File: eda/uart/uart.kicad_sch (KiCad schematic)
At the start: 15 parts, among them J1 UART, U10 74HCT574, U15 74HCT00, U16 74HCT139, U18 74HCT32, U2 74HCT14, U6 74HCT08

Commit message: Branch of uart to v1
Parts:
- removed H1, H2: MountingHole, MountingHole:MountingHole_2.5mm, symbol Mechanical:MountingHole
- removed unit 6 of U2
- added H1, H2, H3, H4, H5, H6: MountingHole_Pad, MountingHole:MountingHole_2.5mm_Pad_Via, symbol Mechanical:MountingHole_Pad
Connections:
- net GND: now also H1.1, H2.1, H3.1, H4.1, H5.1, H6.1
- no-connect marks 8 -> 7

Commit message: Normalize cap size
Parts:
- C1, C15, C18, C19, C2, C21: footprint Capacitor_THT:C_Rect_L7.2mm_W3.5mm_P5.00mm_FKS2_FKP2_MKS2_MKP2 -> Capacitor_THT:C_Disc_D3.8mm_W2.6mm_P2.50mm
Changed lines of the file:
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@@
       (effects (font (size 1.27 1.27)) (justify left))
     )
-    (property "Footprint" "Capacitor_THT:C_Rect_L7.2mm_W3.5mm_P5.00mm_FKS2_FKP2_MKS2_MKP2" (at 149.5552 176.53 0)
+    (property "Footprint" "Capacitor_THT:C_Disc_D3.8mm_W2.6mm_P2.50mm" (at 149.5552 176.53 0)
       (effects (font (size 1.27 1.27)) hide)
     )
@@
       (effects (font (size 1.27 1.27)) (justify left))
     )
-    (property "Footprint" "Capacitor_THT:C_Rect_L7.2mm_W3.5mm_P5.00mm_FKS2_FKP2_MKS2_MKP2" (at 122.8852 176.53 0)
+    (property "Footprint" "Capacitor_THT:C_Disc_D3.8mm_W2.6mm_P2.50mm" (at 122.8852 176.53 0)
       (effects (font (size 1.27 1.27)) hide)
     )
@@
       (effects (font (size 1.27 1.27)) (justify left))
     )
-    (property "Footprint" "Capacitor_THT:C_Rect_L7.2mm_W3.5mm_P5.00mm_FKS2_FKP2_MKS2_MKP2" (at 18.7452 175.895 0)
+    (property "Footprint" "Capacitor_THT:C_Disc_D3.8mm_W2.6mm_P2.50mm" (at 18.7452 175.895 0)
       (effects (font (size 1.27 1.27)) hide)
     )
@@
       (effects (font (size 1.27 1.27)) (justify left))
     )
-    (property "Footprint" "Capacitor_THT:C_Rect_L7.2mm_W3.5mm_P5.00mm_FKS2_FKP2_MKS2_MKP2" (at 55.5752 175.895 0)
+    (property "Footprint" "Capacitor_THT:C_Disc_D3.8mm_W2.6mm_P2.50mm" (at 55.5752 175.895 0)
       (effects (font (size 1.27 1.27)) hide)
     )
@@
       (effects (font (size 1.27 1.27)) (justify left))
     )
-    (property "Footprint" "Capacitor_THT:C_Rect_L7.2mm_W3.5mm_P5.00mm_FKS2_FKP2_MKS2_MKP2" (at 93.0402 175.895 0)
+    (property "Footprint" "Capacitor_THT:C_Disc_D3.8mm_W2.6mm_P2.50mm" (at 93.0402 175.895 0)
       (effects (font (size 1.27 1.27)) hide)
     )
@@
       (effects (font (size 1.27 1.27)) (justify left))
     )
-    (property "Footprint" "Capacitor_THT:C_Rect_L7.2mm_W3.5mm_P5.00mm_FKS2_FKP2_MKS2_MKP2" (at 272.7452 53.34 0)
-      (effects (font (size 1.27 1.27)) hide)
-    )
+    (property "Footprint" "Capacitor_THT:C_Disc_D3.8mm_W2.6mm_P2.50mm" (at 272.7452 53.34 0)
+      (effects (font (size 1.27 1.27)) hide)
+    )

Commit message: Uart and loader work
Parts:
- renumbered U6 to U1, U16 to U7
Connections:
- net GND: now also U10.3 (D1), U10.4 (D2); no longer U10.8 (D6), U10.9 (D7)
- net recieve/DataAvailable: now also U10.9 (D7); no longer U10.4 (D2)
- net recieve/RecieveBufferFull: now also U10.2 (D0); no longer U10.3 (D1)
- net transmit/InputBufferFull: now also U10.8 (D6); no longer U10.2 (D0)

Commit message: Uart eda work
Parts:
- removed J1: UART, Connector_PinHeader_2.54mm:PinHeader_1x03_P2.54mm_Horizontal, symbol Connector:Conn_01x03_Pin
- added C22: 0.1uf, Capacitor_THT:C_Disc_D3.8mm_W2.6mm_P2.50mm, symbol Device:C
- added J1: RX/TX Con, Connector_PinHeader_2.54mm:PinHeader_1x04_P2.54mm_Horizontal, symbol Connector:Conn_01x04_Pin
- added JP9: IRQ Disconnect, Connector_PinHeader_2.54mm:PinHeader_1x02_P2.54mm_Vertical, symbol Jumper:Jumper_2_Bridged
- added U19: 74HCT74, Package_DIP:DIP-14_W7.62mm, symbol 74xx:74HC74
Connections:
- net Expansion header/~{IRQ}: now also JP9.1 (A)
- net GND: now also C22.2, J1.4 (Pin_4), U19.11 (C), U19.12 (D), U19.7 (GND); no longer U10.3 (D1), U15.4, U15.5
- net VCC: now also C22.1, U19.14 (VCC)
- net recieve/DataAvailable: now also U15.4
- net recieve/RX: now also J1.3 (Pin_3)
- net transmit/TX: now also J1.2 (Pin_2)
- net at U15.6: now also U19.10 (~{S})
- new net: U10.3 (D1), U19.9 (Q)
- new net: JP9.2 (B), U19.8 (~{Q})
- new net address_decode/IrqActive: U15.5
- new net address_decode/~{DeviceEnable}: U19.13 (~{R})
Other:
- sheet address_decode ports: added D0, IrqActive, ~{DeviceEnable}, ~{RST}; removed none
- moved on the sheet: C1, C18, C19, C21, U15B, U15E, U16C, U18C, U18D, U18E, U1E, U2C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

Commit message: UART routing pass 1
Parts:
- removed H1, H2: MountingHole_Pad, MountingHole:MountingHole_2.5mm_Pad_Via, symbol Mechanical:MountingHole_Pad
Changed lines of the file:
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@@
 	)
 	(junction
-		(at 146.05 60.96)
+		(at 148.59 30.48)
 		(diameter 0)
 		(color 0 0 0 0)
 	)
 	(junction
-		(at 255.27 118.11)
+		(at 146.05 60.96)
 		(diameter 0)
 		(color 0 0 0 0)
 	)
 	(junction
-		(at 39.878 101.346)
+		(at 255.27 118.11)
 		(diameter 0)
 		(color 0 0 0 0)
@@
 	)
 	(junction
-		(at 39.878 110.49)
+		(at 100.33 39.37)
 		(diameter 0)
 		(color 0 0 0 0)
 	)
 	(junction
-		(at 100.33 39.37)
+		(at 148.59 19.05)
 		(diameter 0)
 		(color 0 0 0 0)
@@
 	(wire
 		(pts
-			(xy 39.878 92.202) (xy 39.878 101.346)
-		)
-		(stroke
-			(width 0)
-			(type default)
-		)
-	)
-	(wire
-		(pts
 			(xy 102.87 156.21) (xy 102.87 157.48)
 		)
@@
 		)
 	)
+	(bus
+		(pts
+			(xy 148.59 30.48) (xy 148.59 57.15)
+		)
+		(stroke
+			(width 0)
+			(type default)
+		)
+	)
 	(wire
 		(pts
@@
 	(bus
 		(pts
-			(xy 95.25 19.05) (xy 262.89 19.05)
+			(xy 95.25 19.05) (xy 148.59 19.05)
 		)
 		(stroke
@@
 	(wire
 		(pts
-			(xy 39.878 101.346) (xy 39.878 110.49)
-		)
-		(stroke
-			(width 0)
-			(type default)
-		)
-	)
-	(wire
-		(pts
 			(xy 115.57 157.48) (xy 115.57 167.64)
 		)
@@
 	(wire
 		(pts
-			(xy 29.464 92.202) (xy 39.878 92.202)
-		)
-		(stroke
-			(width 0)
-			(type default)
-		)
-	)
-	(wire
-		(pts
 			(xy 39.878 119.888) (xy 39.878 129.286)
 		)
@@
 	(bus
 		(pts
-			(xy 148.59 19.05) (xy 148.59 57.15)
+			(xy 148.59 19.05) (xy 148.59 30.48)
 		)
 		(stroke
@@
 		)
 	)
-	(wire
+	(bus
 		(pts
-			(xy 29.464 101.346) (xy 39.878 101.346)
+			(xy 148.59 19.05) (xy 262.89 19.05)
 		)
 		(stroke
@@
 	)
 	(symbol
-		(lib_id "Mechanical:MountingHole_Pad")
-		(at 26.924 101.346 90)
-		(unit 1)
-		(exclude_from_sim no)
-		(in_bom yes)
-		(on_board yes)
-		(dnp no)
-		(fields_autoplaced yes)
-		(property "Reference" "H2"
-			(at 25.654 95.504 90)
-			(effects
-				(font
-					(size 1.27 1.27)
-				)
-			)
-		)
-		(property "Value" "MountingHole_Pad"
-			(at 25.654 98.044 90)
-			(effects
-				(font
-					(size 1.27 1.27)
-				)
-			)
-		)
-		(property "Footprint" "MountingHole:MountingHole_2.5mm_Pad_Via"
-			(at 26.924 101.346 0)
-			(effects
-				(font
-					(size 1.27 1.27)
-				)
-				(hide yes)
-			)
-		)
-		(property "Datasheet" "~"
-			(at 26.924 101.346 0)
-			(effects
-				(font
-					(size 1.27 1.27)
-				)
-				(hide yes)
-			)
-		)
-		(property "Description" ""
-			(at 26.924 101.346 0)
-			(effects
-				(font
-					(size 1.27 1.27)
-				)
-				(hide yes)
-			)
-		)
-		(pin "1"
-		)
-		(instances
-			(project "uart"
-				(path "/11545594-d6d6-4b37-a578-fa23933d5773"
-					(reference "H2")
-					(unit 1)
-				)
-			)
-		)
-	)
-	(symbol
 		(lib_id "power:GND")
 		(at 45.72 67.31 270)
@@
 					(unit 1)
 				)
-			)
-		)
-	)
-	(symbol
-		(lib_id "Mechanical:MountingHole_Pad")
-		(at 26.924 92.202 90)
-		(unit 1)
-		(exclude_from_sim no)
-		(in_bom yes)
-		(on_board yes)
-		(dnp no)
-		(fields_autoplaced yes)
-		(property "Reference" "H1"
-			(at 25.654 86.36 90)
-			(effects
-				(font
-					(size 1.27 1.27)
-				)
-			)
-		)
-		(property "Value" "MountingHole_Pad"
-			(at 25.654 88.9 90)
-			(effects
-				(font
-					(size 1.27 1.27)
-				)
-			)
-		)
-		(property "Footprint" "MountingHole:MountingHole_2.5mm_Pad_Via"
-			(at 26.924 92.202 0)
-			(effects
-				(font
-					(size 1.27 1.27)
-				)
-				(hide yes)
-			)
-		)
-		(property "Datasheet" "~"
-			(at 26.924 92.202 0)
-			(effects
-				(font
-					(size 1.27 1.27)
-				)
-				(hide yes)
-			)
-		)
-		(property "Description" ""
-			(at 26.924 92.202 0)
-			(effects
-				(font
-					(size 1.27 1.27)
-				)
-				(hide yes)
-			)
-		)
-		(pin "1"
-		)
-		(instances
-			(project "uart"
-				(path "/11545594-d6d6-4b37-a578-fa23933d5773"
-					(reference "H1")
-					(unit 1)
-				)

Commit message: Uart latch logic
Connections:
- net Expansion header/Clock: now also U7.14 (A0); no longer U10.11 (Cp)
- net GND: now also U7.15 (E); no longer U7.14 (A0)
- net VCC: no longer U7.15 (E)
- net at U7.11 (O1): now also U10.11 (Cp)
- no-connect marks 7 -> 6
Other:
- moved on the sheet: U7B
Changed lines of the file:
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@@
 	)
 	(junction
+		(at 224.79 99.06)
+		(diameter 0)
+		(color 0 0 0 0)
+	)
+	(junction
 		(at 148.59 30.48)
 		(diameter 0)
@@
 	)
 	(junction
-		(at 255.27 142.24)
-		(diameter 0)
-		(color 0 0 0 0)
-	)
-	(junction
 		(at 102.87 185.42)
 		(diameter 0)
@@
 	)
 	(junction
-		(at 255.27 139.7)
-		(diameter 0)
-		(color 0 0 0 0)
-	)
-	(junction
 		(at 223.52 48.26)
 		(diameter 0)
@@
 	)
 	(no_connect
-		(at 283.21 142.24)
+		(at 251.46 91.44)
 	)
 	(no_connect
@@
 	)
 	(no_connect
-		(at 283.21 144.78)
-	)
-	(no_connect
-		(at 283.21 147.32)
+		(at 251.46 96.52)
 	)
 	(no_connect
-		(at 283.21 139.7)
+		(at 251.46 99.06)
 	)
 	(no_connect
@@
 	(wire
 		(pts
+			(xy 233.68 82.55) (xy 255.27 82.55)
+		)
+		(stroke
+			(width 0)
+			(type default)
+		)
+	)
+	(wire
+		(pts
 			(xy 130.81 185.42) (xy 130.81 186.69)
 		)
@@
 	(wire
 		(pts
+			(xy 226.06 60.96) (xy 224.79 60.96)
+		)
+		(stroke
+			(width 0)
+			(type default)
+		)
+	)
+	(wire
+		(pts
 			(xy 77.47 62.23) (xy 80.01 62.23)
 		)
@@
 	(wire
 		(pts
+			(xy 224.79 99.06) (xy 226.06 99.06)
+		)
+		(stroke
+			(width 0)
+			(type default)
+		)
+	)
+	(wire
+		(pts
 			(xy 146.05 34.29) (xy 146.05 60.96)
 		)
@@
 	(wire
 		(pts
-			(xy 255.27 142.24) (xy 255.27 158.75)
+			(xy 255.27 130.81) (xy 255.27 158.75)
 		)
 		(stroke
@@
 	(wire
 		(pts
+			(xy 226.06 90.17) (xy 222.25 90.17)
+		)
+		(stroke
+			(width 0)
+			(type default)
+		)
+	)
+	(wire
+		(pts
+			(xy 222.25 90.17) (xy 222.25 93.98)
+		)
+		(stroke
+			(width 0)
+			(type default)
+		)
+	)
+	(wire
+		(pts
+			(xy 233.68 78.74) (xy 233.68 82.55)
+		)
+		(stroke
+			(width 0)
+			(type default)
+		)
+	)
+	(wire
+		(pts
+			(xy 224.79 99.06) (xy 224.79 104.14)
+		)
+		(stroke
+			(width 0)
+			(type default)
+		)
+	)
+	(wire
+		(pts
 			(xy 255.27 125.73) (xy 255.27 130.81)
 		)
@@
 	(wire
 		(pts
-			(xy 200.66 80.01) (xy 200.66 60.96)
+			(xy 224.79 91.44) (xy 224.79 99.06)
 		)
 		(stroke
@@
 	(wire
 		(pts
-			(xy 255.27 139.7) (xy 255.27 142.24)
-		)
-		(stroke
-			(width 0)
-			(type default)
-		)
-	)
-	(wire
-		(pts
 			(xy 80.01 62.23) (xy 81.28 62.23)
 		)
@@
 	(wire
 		(pts
-			(xy 200.66 60.96) (xy 226.06 60.96)
-		)
-		(stroke
-			(width 0)
-			(type default)
-		)
-	)
-	(wire
-		(pts
 			(xy 54.61 113.03) (xy 69.85 113.03)
 		)
@@
 	(wire
 		(pts
-			(xy 255.27 139.7) (xy 257.81 139.7)
-		)
-		(stroke
-			(width 0)
-			(type default)
-		)
-	)
-	(wire
-		(pts
 			(xy 102.87 157.48) (xy 102.87 158.75)
 		)
@@
 	(wire
 		(pts
-			(xy 255.27 130.81) (xy 255.27 139.7)
-		)
-		(stroke
-			(width 0)
-			(type default)
-		)
-	)
-	(wire
-		(pts
 			(xy 44.45 25.4) (xy 48.26 25.4)
 		)
@@
 	(wire
 		(pts
-			(xy 255.27 142.24) (xy 257.81 142.24)
+			(xy 255.27 82.55) (xy 255.27 93.98)
 		)
 		(stroke
@@
 	(wire
 		(pts
-			(xy 100.33 80.01) (xy 200.66 80.01)
+			(xy 100.33 80.01) (xy 226.06 80.01)
 		)
 		(stroke
@@
 	(wire
 		(pts
+			(xy 224.79 78.74) (xy 233.68 78.74)
+		)
+		(stroke
+			(width 0)
+			(type default)
+		)
+	)
+	(wire
+		(pts
 			(xy 238.76 73.66) (xy 238.76 72.39)
 		)
@@
 	(wire
 		(pts
+			(xy 251.46 93.98) (xy 255.27 93.98)
+		)
+		(stroke
+			(width 0)
+			(type default)
+		)
+	)
+	(wire
+		(pts
+			(xy 222.25 93.98) (xy 226.06 93.98)
+		)
+		(stroke
+			(width 0)
+			(type default)
+		)
+	)
+	(wire
+		(pts
 			(xy 156.21 182.88) (xy 156.21 185.42)
 		)
@@
 		)
 	)
+	(wire
+		(pts
+			(xy 226.06 91.44) (xy 224.79 91.44)
+		)
+		(stroke
+			(width 0)
+			(type default)
+		)
+	)
+	(wire
+		(pts
+			(xy 224.79 60.96) (xy 224.79 78.74)
+		)
+		(stroke
+			(width 0)
+			(type default)
+		)
+	)
 	(bus
 		(pts
@@
 		)
 	)
+	(wire
+		(pts
+			(xy 226.06 80.01) (xy 226.06 90.17)
+		)
+		(stroke
+			(width 0)
+			(type default)
+		)
+	)
 	(label "D5"
 		(at 251.46 50.8 0)
@@
 	(label "D0"
 		(at 100.33 26.67 0)
+		(fields_autoplaced yes)
 		(effects
 			(font
@@
 	)
 	(symbol
-		(lib_id "power:VCC")
-		(at 257.81 147.32 180)
-		(unit 1)
-		(exclude_from_sim no)
-		(in_bom yes)
-		(on_board yes)
-		(dnp no)
-		(fields_autoplaced yes)
-		(property "Reference" "#PWR053"
-			(at 257.81 143.51 0)
-			(effects
-				(font
-					(size 1.27 1.27)
-				)
-				(hide yes)
-			)
-		)
-		(property "Value" "VCC"
-			(at 257.81 152.4 0)
-			(effects
-				(font
-					(size 1.27 1.27)
-				)
-			)
-		)
-		(property "Footprint" ""
-			(at 257.81 147.32 0)
-			(effects
-				(font
-					(size 1.27 1.27)
-				)
-				(hide yes)
-			)
-		)
-		(property "Datasheet" ""
-			(at 257.81 147.32 0)
-			(effects
-				(font
-					(size 1.27 1.27)
-				)
-				(hide yes)
-			)
-		)
-		(property "Description" ""
-			(at 257.81 147.32 0)
-			(effects
-				(font
-					(size 1.27 1.27)
-				)
-				(hide yes)
-			)
-		)
-		(pin "1"
-		)
-		(instances
-			(project "uart"
-				(path "/11545594-d6d6-4b37-a578-fa23933d5773"
-					(reference "#PWR053")
-					(unit 1)
-				)
-			)
-		)
-	)
-	(symbol
 		(lib_id "power:GND")
 		(at 69.85 142.24 0)
@@
 	(symbol
 		(lib_id "74xx:74LS139")
-		(at 270.51 142.24 0)
+		(at 238.76 93.98 0)
 		(unit 2)
 		(exclude_from_sim no)
@@
 		(fields_autoplaced yes)
 		(property "Reference" "U7"
-			(at 270.51 133.35 0)
+			(at 238.76 85.09 0)
 			(effects
 				(font
@@
 		)
 		(property "Value" "74HCT139"
-			(at 270.51 135.89 0)
+			(at 238.76 87.63 0)
 			(effects
 				(font
@@
 		)
 		(property "Footprint" "Package_DIP:DIP-16_W7.62mm"
-			(at 270.51 142.24 0)
+			(at 238.76 93.98 0)
 			(effects
 				(font
@@
 		)
 		(property "Datasheet" "http://www.ti.com/lit/ds/symlink/sn74ls139a.pdf"
-			(at 270.51 142.24 0)
+			(at 238.76 93.98 0)
 			(effects
 				(font
@@
 		)
 		(property "Description" ""
-			(at 270.51 142.24 0)
+			(at 238.76 93.98 0)
 			(effects
 				(font
@@
 					(unit 1)
 				)
+			)
+		)
+	)
+	(symbol
+		(lib_id "power:GND")
+		(at 224.79 104.14 0)
+		(unit 1)
+		(exclude_from_sim no)
+		(in_bom yes)
+		(on_board yes)
+		(dnp no)
+		(fields_autoplaced yes)
+		(property "Reference" "#PWR053"
+			(at 224.79 110.49 0)
+			(effects
+				(font
+					(size 1.27 1.27)
+				)
+				(hide yes)
+			)
+		)
+		(property "Value" "GND"
+			(at 224.79 109.22 0)
+			(effects
+				(font
+					(size 1.27 1.27)
+				)
+			)
+		)
+		(property "Footprint" ""
+			(at 224.79 104.14 0)
+			(effects
+				(font
+					(size 1.27 1.27)
+				)
+				(hide yes)
+			)
+		)
+		(property "Datasheet" ""
+			(at 224.79 104.14 0)
+			(effects
+				(font
+					(size 1.27 1.27)
+				)
+				(hide yes)
+			)
+		)
+		(property "Description" ""
+			(at 224.79 104.14 0)
+			(effects
+				(font
+					(size 1.27 1.27)
+				)
+				(hide yes)
+			)
+		)
+		(pin "1"
+		)
+		(instances
+			(project "uart"
+				(path "/11545594-d6d6-4b37-a578-fa23933d5773"
+					(reference "#PWR053")
+					(unit 1)
+				)

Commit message: Touchups before ordering
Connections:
- net recieve/RX: now also J1.2 (Pin_2); no longer J1.3 (Pin_3)
- net transmit/TX: now also J1.3 (Pin_3); no longer J1.2 (Pin_2)

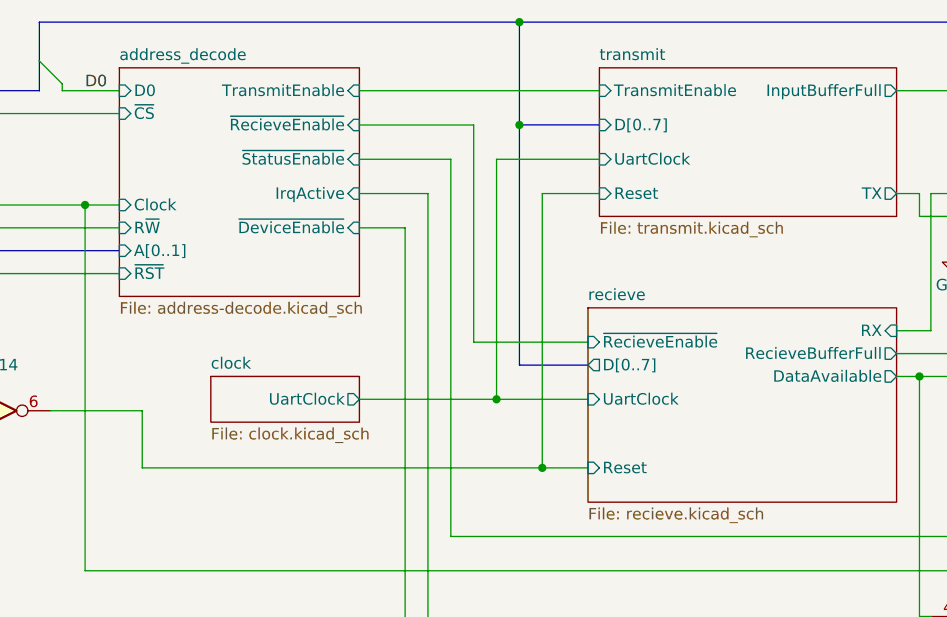
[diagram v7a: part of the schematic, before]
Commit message: Uart board to v1.1...make bodges permanent :(
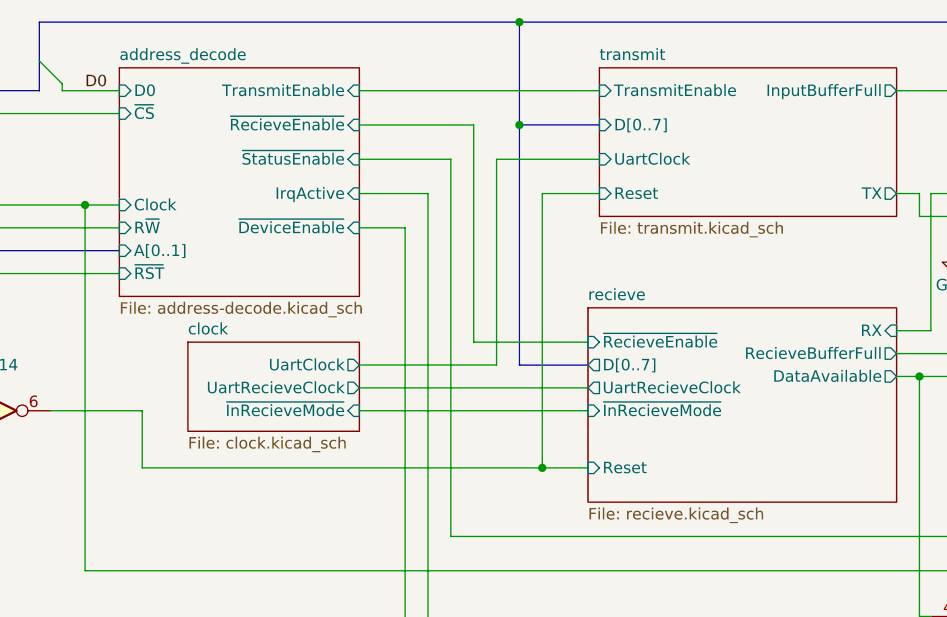
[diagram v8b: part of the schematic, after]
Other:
- sheet clock ports: added UartRecieveClock, ~{InRecieveMode}; removed none
- sheet recieve ports: added UartRecieveClock, ~{InRecieveMode}; removed UartClock
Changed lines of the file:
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@@
 	)
 	(junction
-		(at 146.05 60.96)
-		(diameter 0)
-		(color 0 0 0 0)
-	)
-	(junction
 		(at 255.27 118.11)
 		(diameter 0)
@@
 	(wire
 		(pts
-			(xy 146.05 60.96) (xy 156.21 60.96)
-		)
-		(stroke
-			(width 0)
-			(type default)
-		)
-	)
-	(wire
-		(pts
 			(xy 190.5 55.88) (xy 215.9 55.88)
 		)
@@
 	(wire
 		(pts
-			(xy 146.05 34.29) (xy 146.05 60.96)
+			(xy 146.05 34.29) (xy 146.05 57.15)
 		)
 		(stroke
@@
 	(wire
 		(pts
-			(xy 130.81 60.96) (xy 146.05 60.96)
+			(xy 130.81 57.15) (xy 146.05 57.15)
 		)
 		(stroke
@@
 		)
 	)
+	(wire
+		(pts
+			(xy 130.81 59.69) (xy 156.21 59.69)
+		)
+		(stroke
+			(width 0)
+			(type default)
+		)
+	)
 	(bus
 		(pts
@@
 		)
 	)
+	(wire
+		(pts
+			(xy 130.81 62.23) (xy 156.21 62.23)
+		)
+		(stroke
+			(width 0)
+			(type default)
+		)
+	)
 	(bus
 		(pts
@@
 	)
 	(sheet
-		(at 114.3 58.42)
-		(size 16.51 5.08)
+		(at 111.76 54.61)
+		(size 19.05 9.906)
 		(fields_autoplaced yes)
 		(stroke
@@
 		)
 		(property "Sheetname" "clock"
-			(at 114.3 57.7084 0)
+			(at 111.76 53.8984 0)
 			(effects
 				(font
@@
 		)
 		(property "Sheetfile" "clock.kicad_sch"
-			(at 114.3 64.0846 0)
+			(at 111.76 65.1006 0)
 			(effects
 				(font
@@
 		)
 		(pin "UartClock" output
-			(at 130.81 60.96 0)
+			(at 130.81 57.15 0)
+			(effects
+				(font
+					(size 1.27 1.27)
+				)
+				(justify right)
+			)
+		)
+		(pin "~{InRecieveMode}" input
+			(at 130.81 62.23 0)
+			(effects
+				(font
+					(size 1.27 1.27)
+				)
+				(justify right)
+			)
+		)
+		(pin "UartRecieveClock" output
+			(at 130.81 59.69 0)
 			(effects
 				(font
@@
 			)
 		)
-		(pin "UartClock" input
-			(at 156.21 60.96 180)
-			(effects
-				(font
-					(size 1.27 1.27)
-				)
-				(justify left)
-			)
-		)
 		(pin "Reset" input
 			(at 156.21 68.58 180)
@@
 			)
 		)
+		(pin "UartRecieveClock" output
+			(at 156.21 59.69 180)
+			(effects
+				(font
+					(size 1.27 1.27)
+				)
+				(justify left)
+			)
+		)
+		(pin "~{InRecieveMode}" input
+			(at 156.21 62.23 180)
+			(effects
+				(font
+					(size 1.27 1.27)
+				)
+				(justify left)
+			)
+		)
